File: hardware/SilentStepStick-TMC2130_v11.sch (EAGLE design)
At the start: 26 parts, among them IC1 TMC2130-LA, X1 PASSER-07, X2 PASSER-07

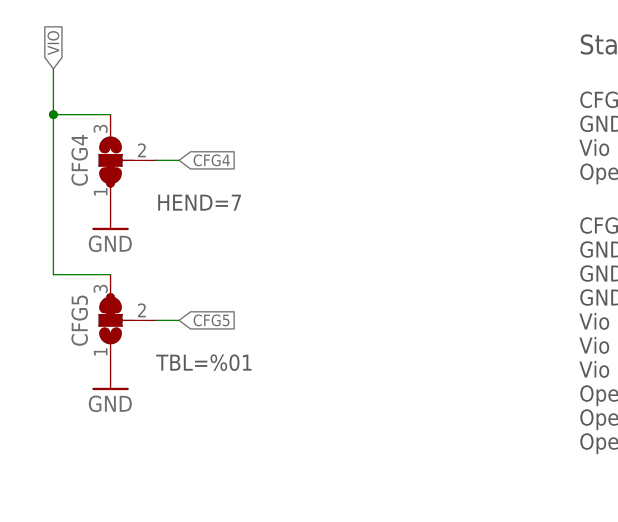
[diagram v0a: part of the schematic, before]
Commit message: updated schematics
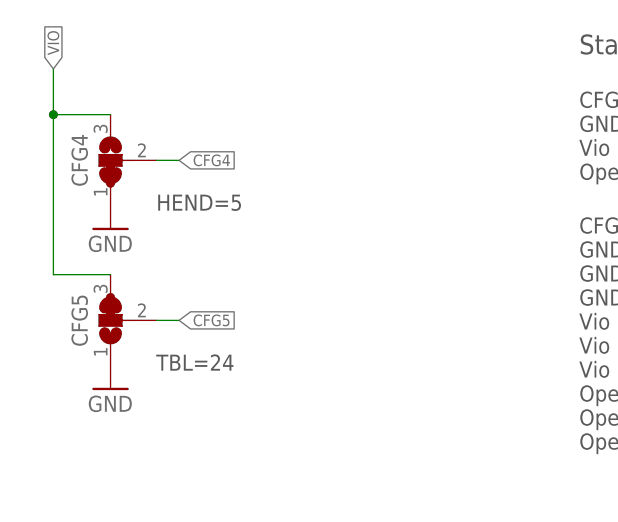
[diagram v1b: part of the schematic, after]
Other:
- note added: "HEND=5"
- note added: "TBL=24"
- note removed: "HEND=7"
- note removed: "TBL=%01"
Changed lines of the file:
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@@
 stealthChop</text>
 <text x="90.17" y="57.15" size="2.1844" layer="97" font="vector" ratio="10" align="top-left">Standalone Operation (SPI_MODE=GND)</text>
-<text x="43.18" y="39.37" size="1.778" layer="97" font="vector" ratio="10" align="top-left">HEND=7</text>
-<text x="43.18" y="21.59" size="1.778" layer="97" font="vector" ratio="10" align="top-left">TBL=%01</text>
+<text x="43.18" y="39.37" size="1.778" layer="97" font="vector" ratio="10" align="top-left">HEND=5</text>
+<text x="43.18" y="21.59" size="1.778" layer="97" font="vector" ratio="10" align="top-left">TBL=24</text>
 </plain>
 <instances>
